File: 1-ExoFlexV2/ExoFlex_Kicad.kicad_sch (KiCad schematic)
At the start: 0 parts

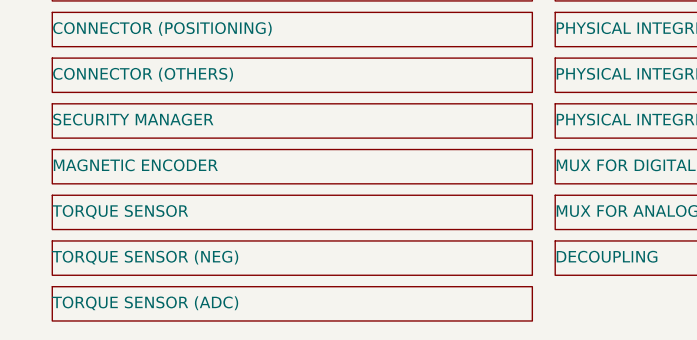
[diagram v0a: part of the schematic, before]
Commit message: Finalisation 2
-Ajout des nouveaux comparateurs
- Ajout d'une page découplage
- Retrait des condensateur dans les autres pages
- Ajout de trimmer pour les résistance importante mais incertaines
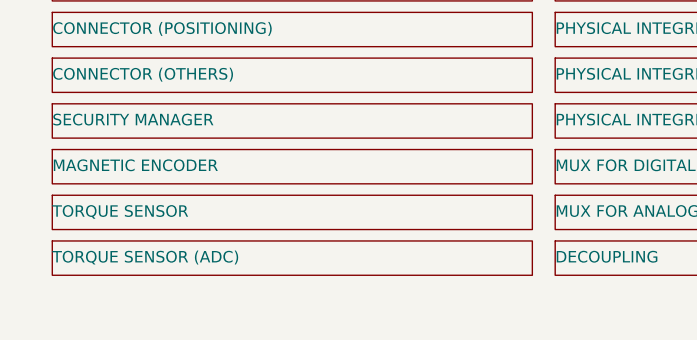
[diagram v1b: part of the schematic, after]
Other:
- removed sheet TORQUE SENSOR (NEG)

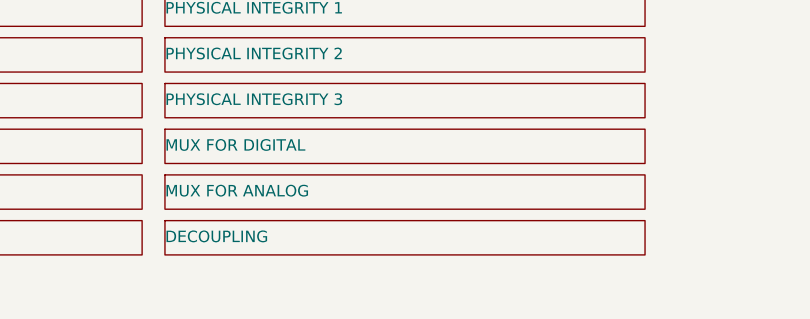
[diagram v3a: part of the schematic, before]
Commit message: Test points et notes
- Ajout de tous les tests point nécessaires
-  Ajoute des sections de notes dans chaque page
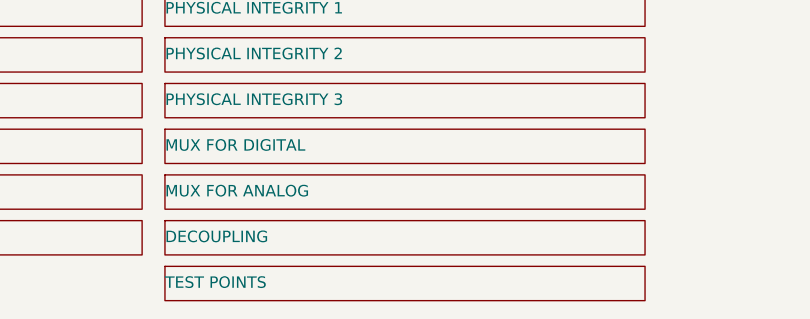
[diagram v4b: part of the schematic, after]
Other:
- added sheet TEST POINTS (testpoint.kicad_sch)
